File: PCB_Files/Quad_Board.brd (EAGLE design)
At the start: 81 x 76.2 mm, 38 parts

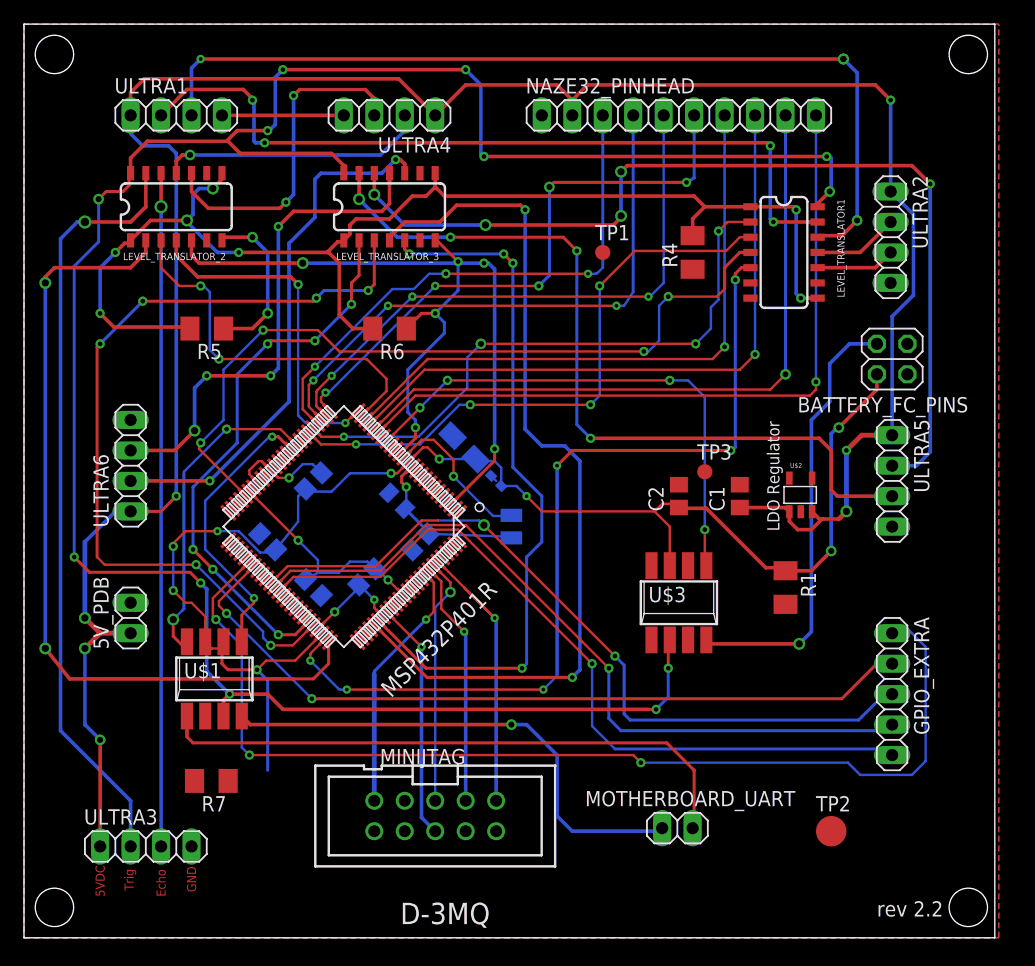
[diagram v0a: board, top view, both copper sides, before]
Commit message: Adding more silscreen info
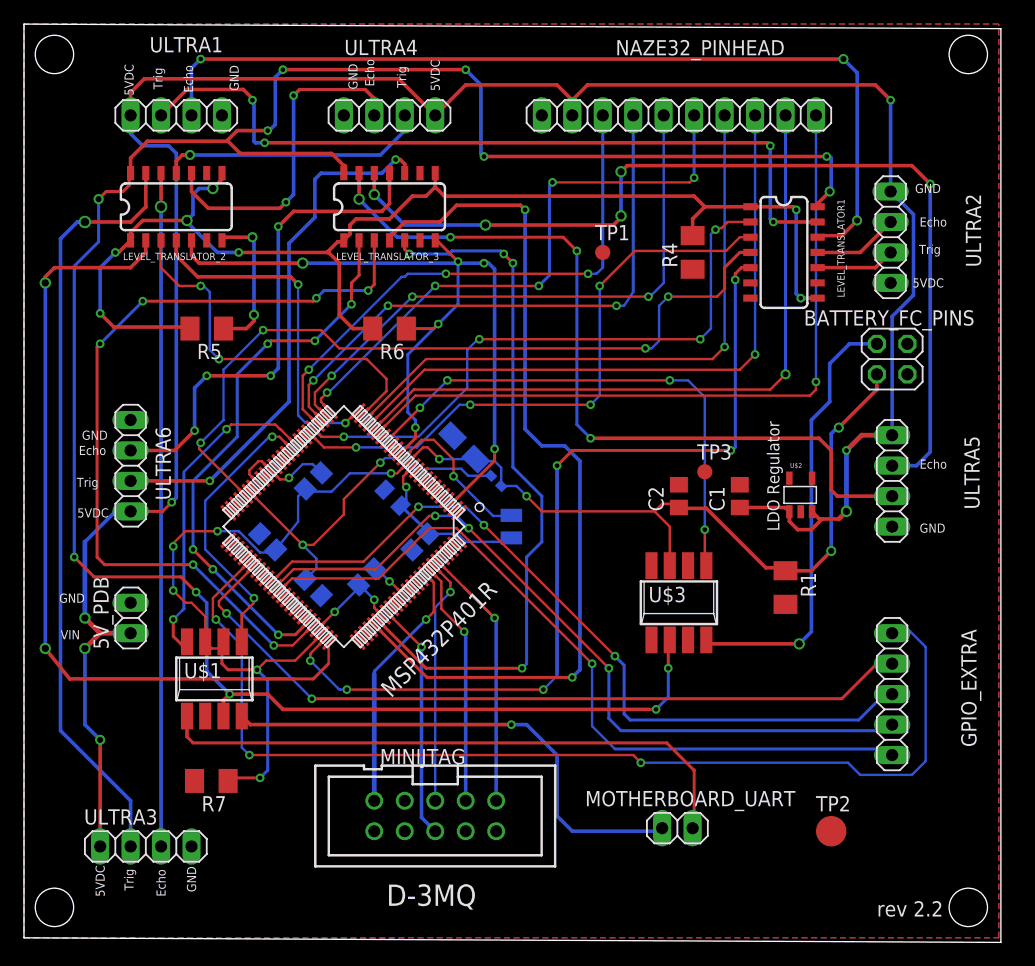
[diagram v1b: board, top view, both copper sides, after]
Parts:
- moved CPOLARIZED 0.46 mm to (30.7, 36.7)
- renumbered CPOLARISED to CPOL
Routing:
- net N$2: track 19.1 -> 38.3 mm, vias 2 -> 3
- net GND: track 66.3 -> 54.3 mm
- net 3V3: track 121.1 -> 124.8 mm, vias 9 -> 10
- net VCORE: track 14.0 -> 15.2 mm
- net P4.5_GPIO: track 64.1 -> 65.1 mm, vias 2 -> 3
- net 5V: track 188.2 -> 187.5 mm
- net P4.6_GPIO: track 63.4 -> 64.0 mm, vias 1 -> 3
- net P8.0: track 50.1 -> 50.7 mm
- net P8.1_5V: vias 4 -> 3
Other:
- board size 81 x 76.2 mm -> 81.5 x 76.6 mm
- board text added: "VIN"
